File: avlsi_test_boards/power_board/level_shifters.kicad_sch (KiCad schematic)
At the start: 13 parts

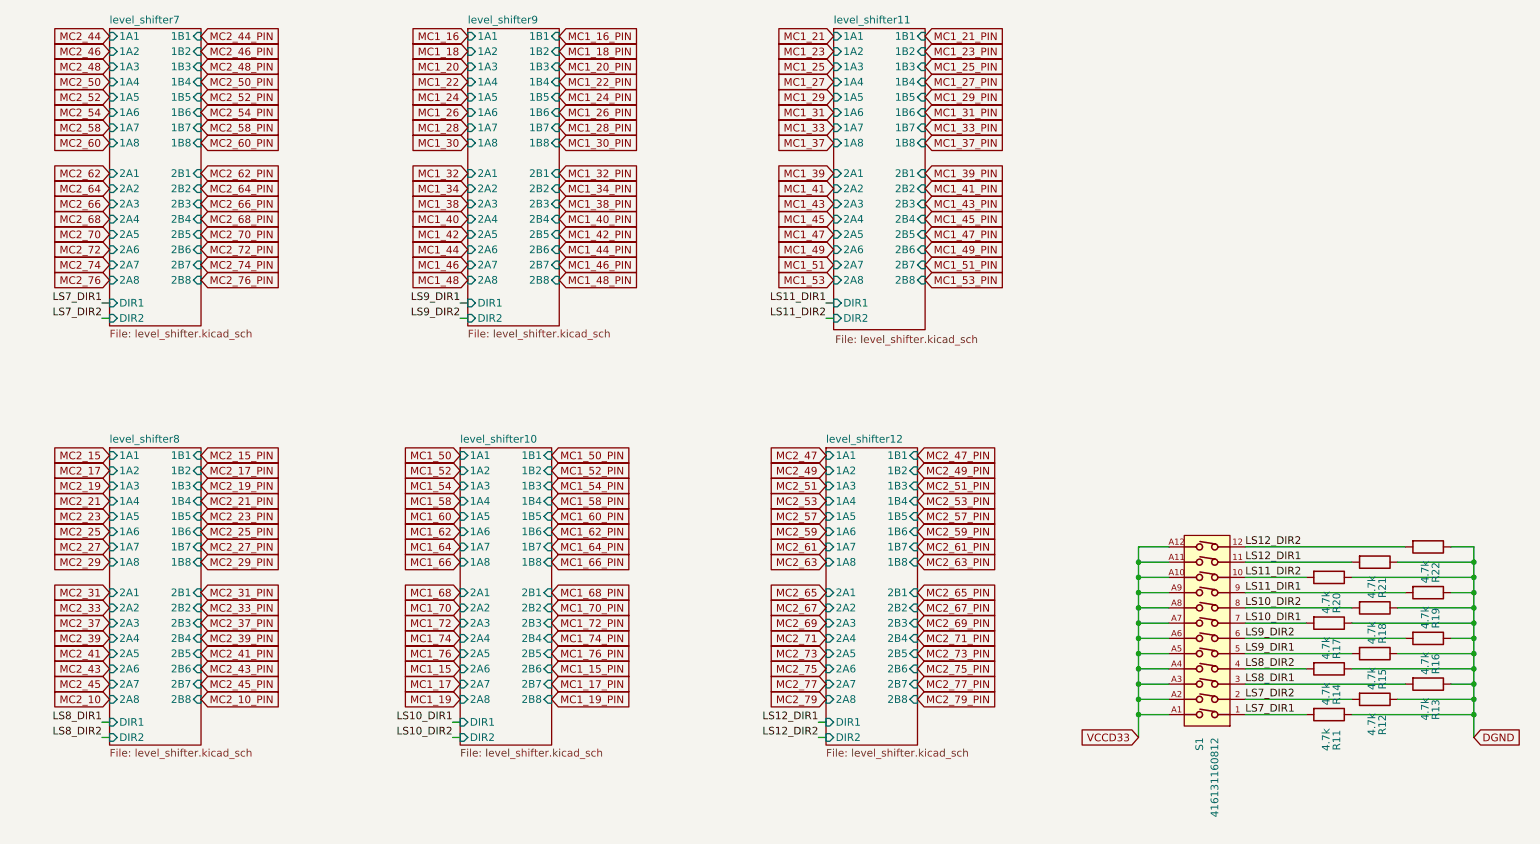
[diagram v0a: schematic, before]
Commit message: Add updated power board layout and schematic
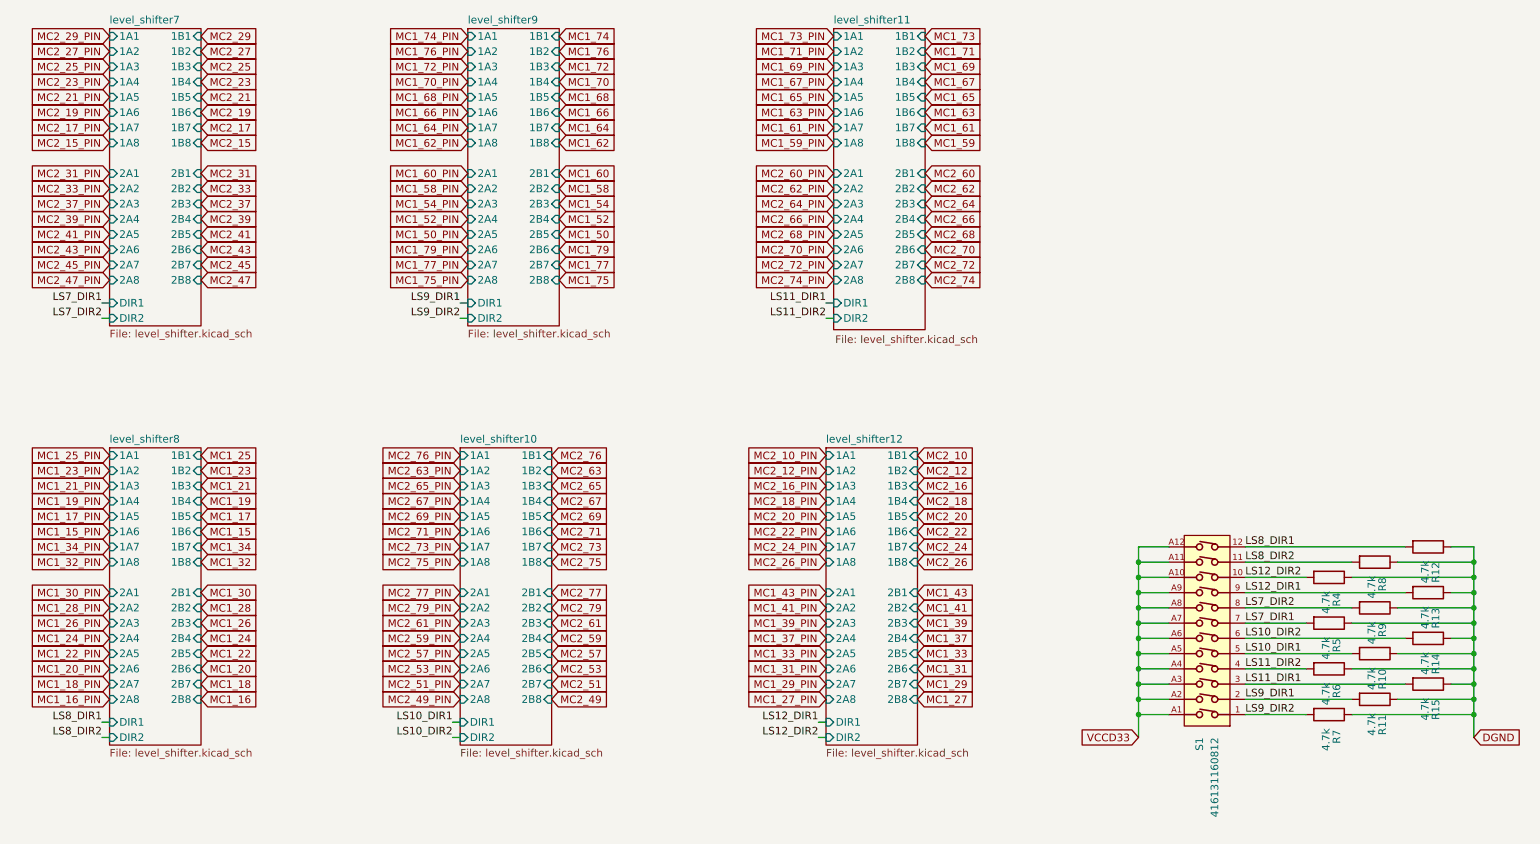
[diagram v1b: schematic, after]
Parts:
- renumbered R15 to R10, R12 to R11, R22 to R12, R19 to R13, R16 to R14, R13 to R15, R20 to R4, R17 to R5, R14 to R6, R11 to R7, R21 to R8, R18 to R9
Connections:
- net LS10_DIR1: now also R10.2, S1.5; no longer R5.2, S1.7
- net LS10_DIR2: now also R14.2, S1.6; no longer R9.2, S1.8
- net LS11_DIR1: now also R15.2, S1.3; no longer R13.2, S1.9
- net LS11_DIR2: now also R6.2, S1.4; no longer R4.2, S1.10
- net LS12_DIR1: now also R13.2, S1.9; no longer R8.2, S1.11
- net LS12_DIR2: now also R4.2, S1.10; no longer R12.2, S1.12
- net LS7_DIR1: now also R5.2, S1.7; no longer R7.2, S1.1
- net LS7_DIR2: now also R9.2, S1.8; no longer R11.2, S1.2
- net LS8_DIR1: now also R12.2, S1.12; no longer R15.2, S1.3
- net LS8_DIR2: now also R8.2, S1.11; no longer R6.2, S1.4
- net LS9_DIR1: now also R11.2, S1.2; no longer R10.2, S1.5
- net LS9_DIR2: now also R7.2, S1.1; no longer R14.2, S1.6

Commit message: Add power board
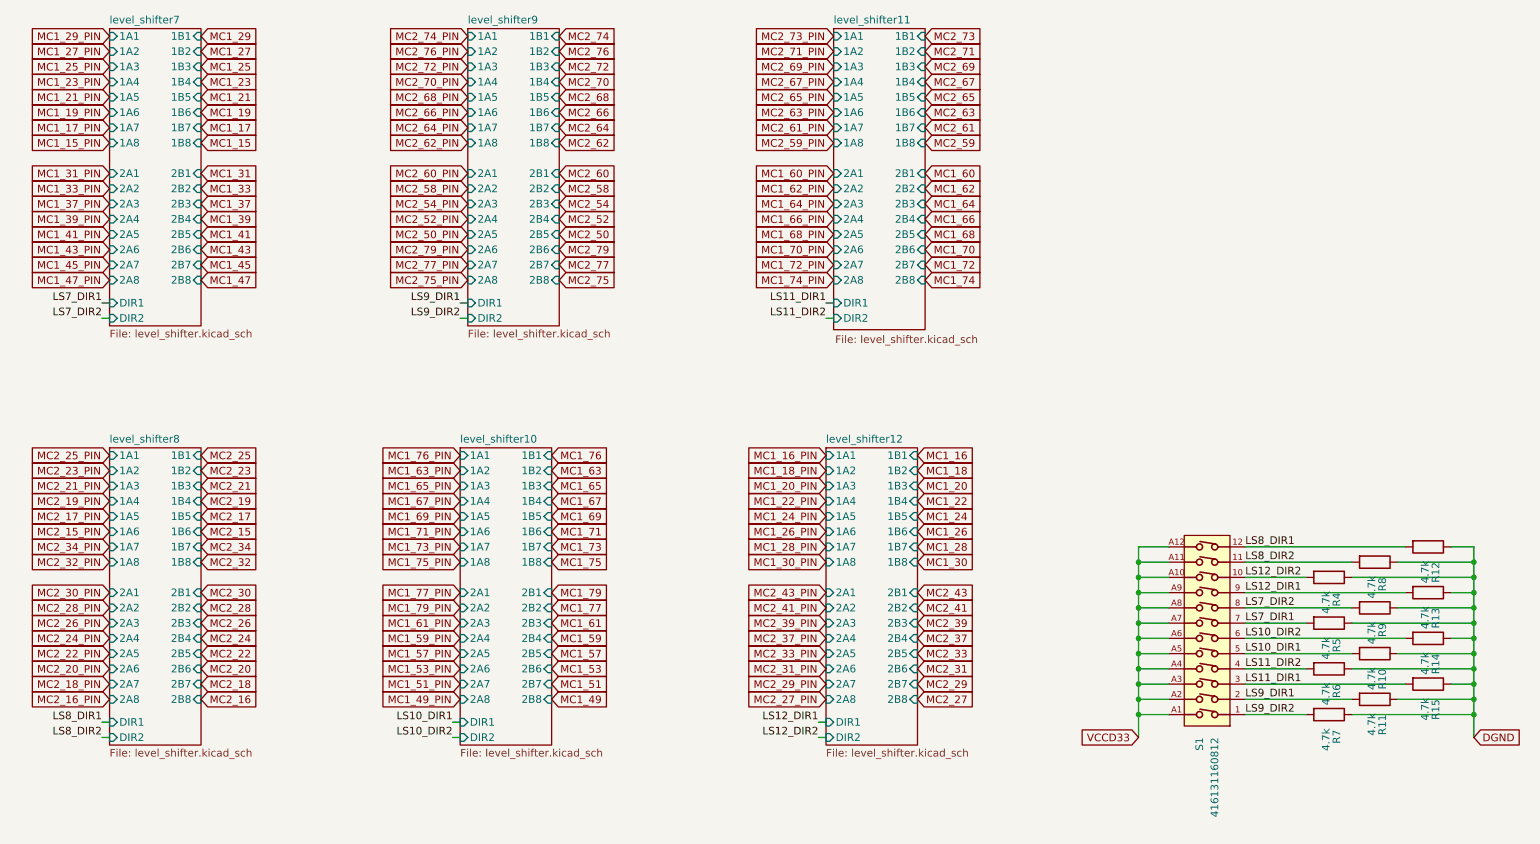
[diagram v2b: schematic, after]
